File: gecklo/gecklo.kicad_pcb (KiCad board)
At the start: 2 copper layers, 22.9 x 22.9 mm, 15 parts, among them J1 Conn_01x09, J2 Conn_01x09, J3 Conn_01x01, J4 USB_B, U1 EFM32HG309, U2 RFM92/95/96/97/98, U3 AP2112_SOT23-5

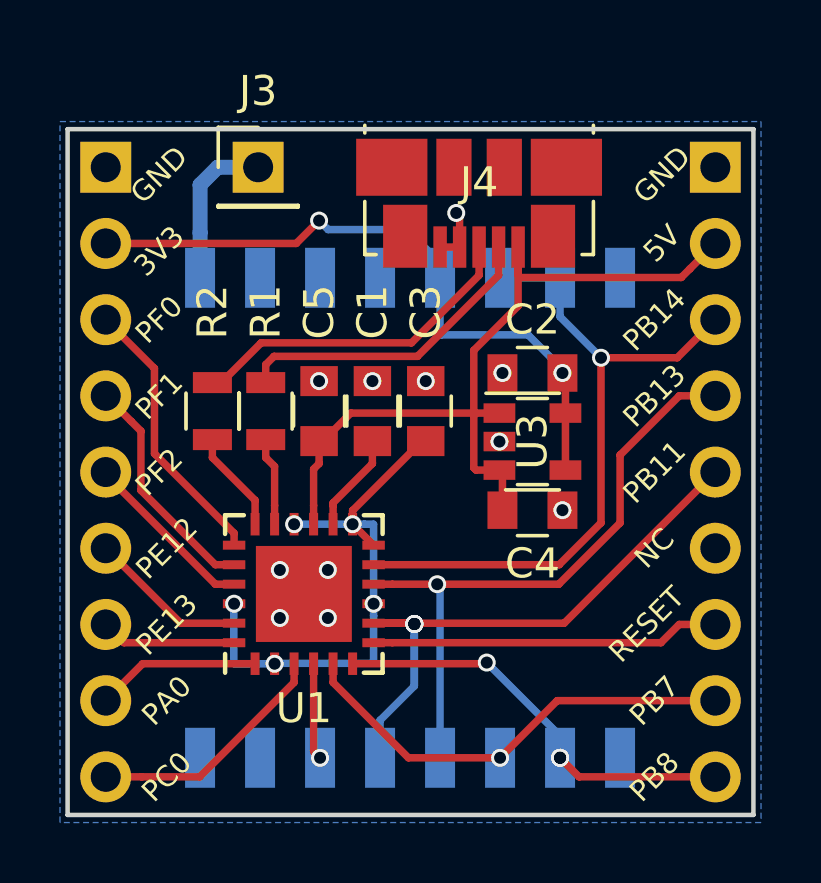
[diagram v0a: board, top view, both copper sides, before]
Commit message: made better gecklo board v0.2
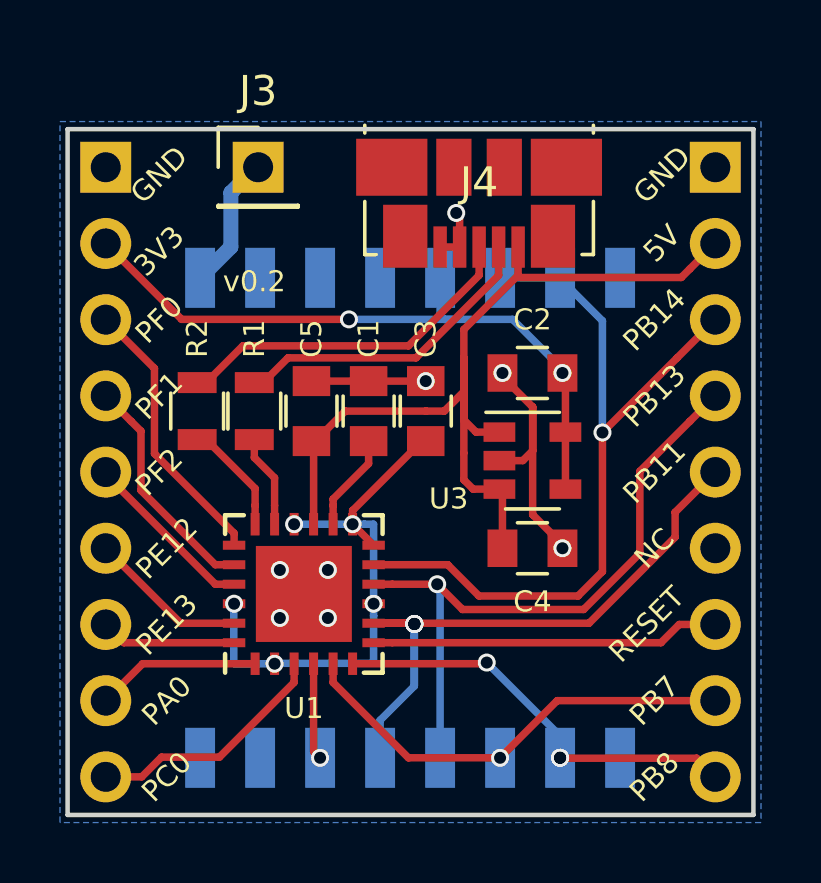
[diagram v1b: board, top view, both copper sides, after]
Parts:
- moved C4 1.27 mm to (153.9, 109.2)
- moved U3 0.64 mm to (153.9, 106.3)
- moved R2 0.51 mm to (142.7, 104.6)
- moved R1 0.38 mm to (144.7, 104.6)
- moved C5 0.25 mm to (146.6, 104.6)
- moved C1 0.13 mm to (148.5, 104.6)
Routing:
- net GND: track 2.65 -> 15.8 mm, vias 11 -> 8
- net +5V: track 27.6 -> 31.0 mm
- net /PB14: track 23.7 -> 26.6 mm
- net /PB13: track 21.1 -> 22.1 mm
- net Net-(J3-Pad1): track 5.28 -> 4.52 mm
- net +3V3: track 23.0 -> 23.7 mm
- net /D+: track 11.3 -> 11.8 mm
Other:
- net class Default: clearance 0.2 -> 0.15
- rule trace_clearance: 0.2 -> 0.15
- board text added: "v0.2"
